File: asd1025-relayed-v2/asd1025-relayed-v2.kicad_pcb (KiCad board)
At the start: 2 copper layers, 61 x 40.6 mm, 20 parts, among them J1 DF3-12S-2DSA, J2 DF3-12S-2DSA, J3 DF3-12S-2DSA, J4 Conn_01x04_Male, J5 Conn_01x01_Female, J6 Conn_01x01_Female, K1 EC2-5NU, K2 EC2-5NU, K3 EC2-5NU, K4 EC2-5NU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

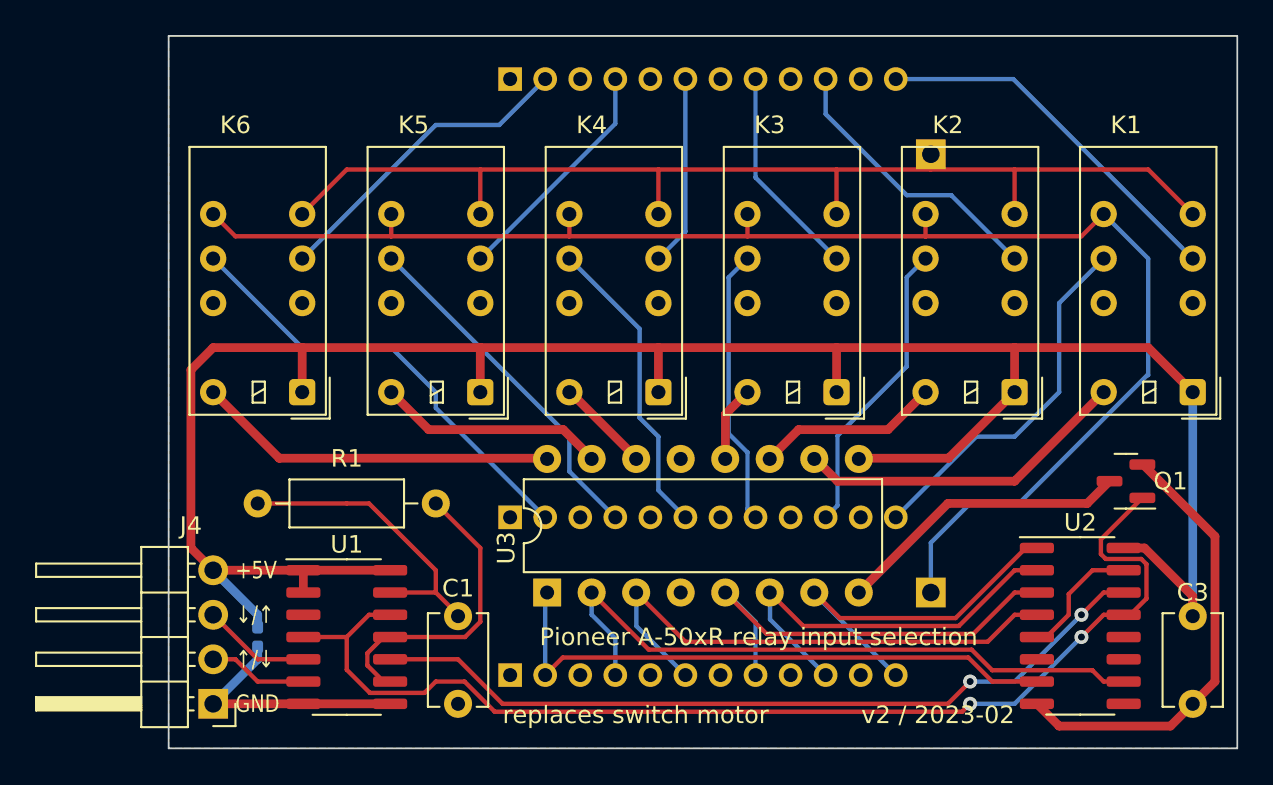
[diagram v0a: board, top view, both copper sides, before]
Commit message: fix mistake in v2 board about oscillator timing logic, nicer bottom silkscreen, no clock enabled signal needed anymore
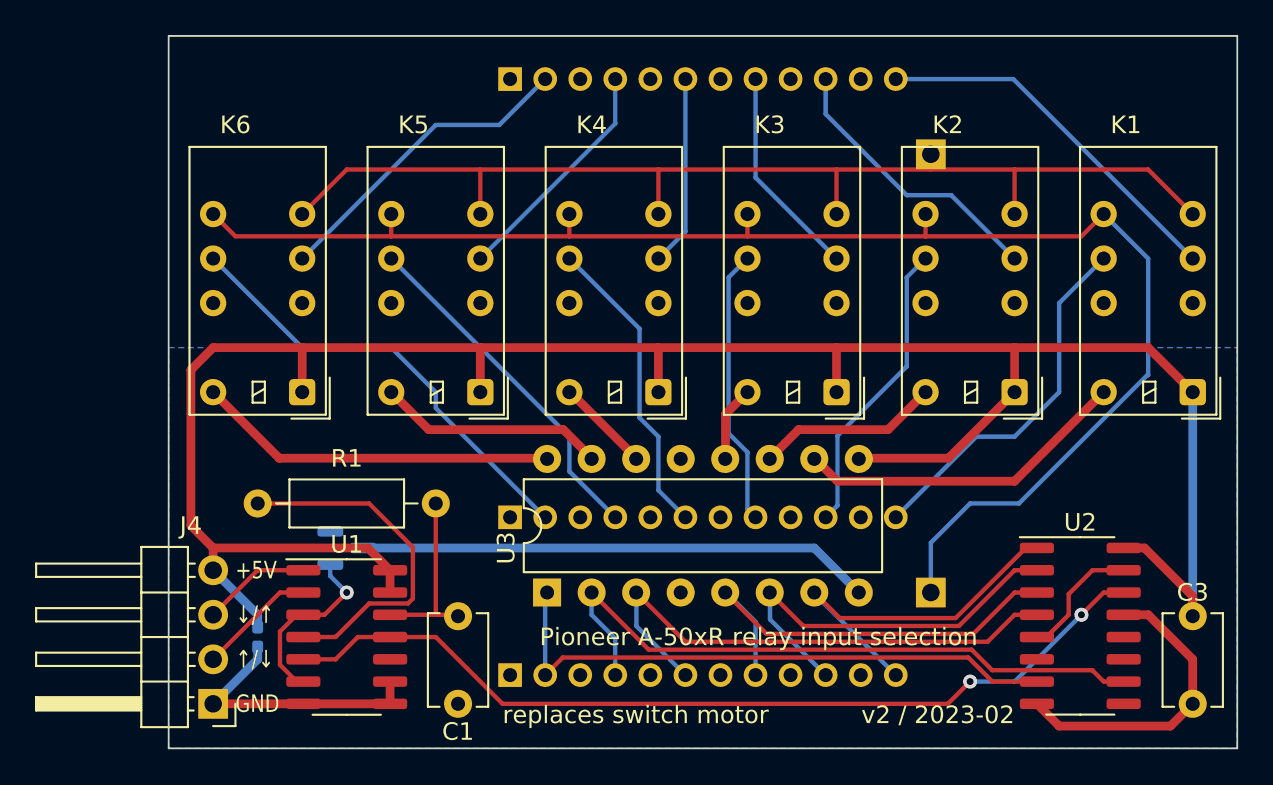
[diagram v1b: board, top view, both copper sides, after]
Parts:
- Q1: moved to B.Cu
- moved Q1 44.6 mm to (91.6, 145.4), turned to 0 degrees
- moved C1 5.00 mm to (97.9, 154.2), turned to 90 degrees
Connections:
- C1 pad 1: Net-(C1-Pad1) -> GNDREF
- C1 pad 2: GNDREF -> Net-(C1-Pad2)
- R1 pad 1: Net-(R1-Pad1) -> Net-(C1-Pad2)
- R1 pad 2: Net-(C1-Pad1) -> Net-(R1-Pad2)
- U1 pad 1: +5V -> Net-(J4-Pad3)
- U1 pad 10: Net-(U2-Pad14) -> unconnected-(U1-Pad10)
- U1 pad 11: Net-(R1-Pad1) -> Net-(U1-Pad11)
- U1 pad 12: Net-(Q1-Pad1) -> Net-(C1-Pad2)
- U1 pad 13: Net-(C1-Pad1) -> +5V
- U1 pad 2: +5V -> Net-(J4-Pad2)
- U1 pad 3: unconnected-(U1-Pad3) -> Net-(Q1-Pad1)
- U1 pad 4: Net-(Q1-Pad1) -> Net-(R1-Pad2)
- U1 pad 5: Net-(J4-Pad3) -> Net-(U1-Pad11)
- U1 pad 6: Net-(J4-Pad2) -> Net-(Q1-Pad1)
- U1 pad 9: Net-(R1-Pad1) -> GNDREF
- U2 pad 13: Net-(Q1-Pad1) -> GNDREF
- U2 pad 14: Net-(U2-Pad14) -> Net-(U1-Pad11)
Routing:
- net Net-(Q1-Pad1): track 66.2 -> 10.3 mm, vias 2 -> 1
- net Net-(U1-Pad11): track 0.00 -> 51.5 mm, vias 0 -> 2
- net Net-(U2-Pad14): track 45.5 -> 0.00 mm, vias 2 -> 0
- net Net-(R1-Pad2): track 0.00 -> 20.0 mm
- net Net-(C1-Pad1): track 17.5 -> 0.00 mm
- net Net-(R1-Pad1): track 17.4 -> 0.00 mm
- net Net-(Q1-Pad3): track 16.9 -> 29.3 mm
- net Net-(C1-Pad2): track 0.00 -> 10.3 mm
- net GNDREF: track 40.2 -> 33.5 mm
- net Net-(J4-Pad2): track 5.67 -> 6.72 mm
- net +5V: track 128.5 -> 129.0 mm

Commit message: change oscillator frequency to minimum to ensure 10ms between relai cut-off and on-switching
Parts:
- R1: value 150k -> 120k
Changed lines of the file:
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@@
       (effects (font (size 1 1) (thickness 0.15)))
     )
-    (fp_text value "150k" (at 5.08 2.37) (layer "F.Fab")
+    (fp_text value "120k" (at 5.08 2.37) (layer "F.Fab")
       (effects (font (size 1 1) (thickness 0.15)))
     )

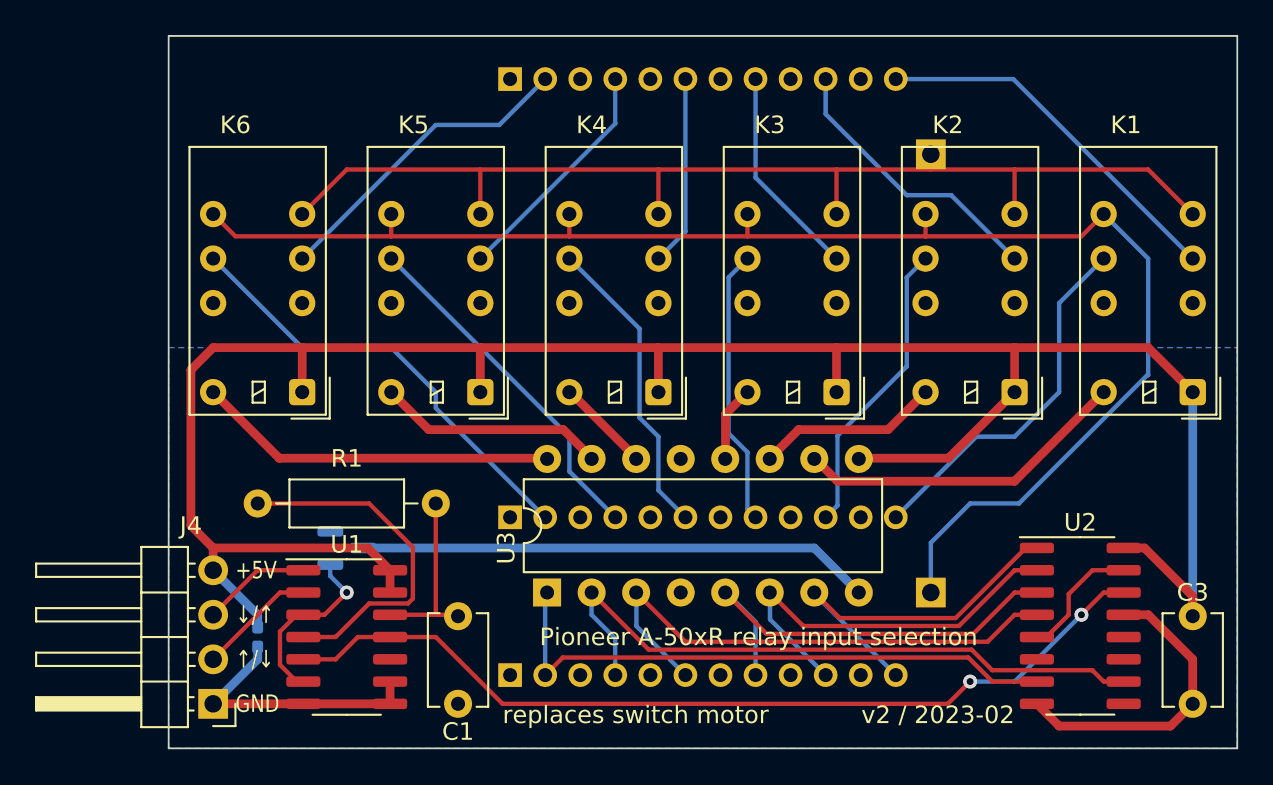
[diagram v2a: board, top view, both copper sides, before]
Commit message: fix v2: relays would switch by passing current through base-emittor-resistors in darlington array even if main transistor Q1 is off
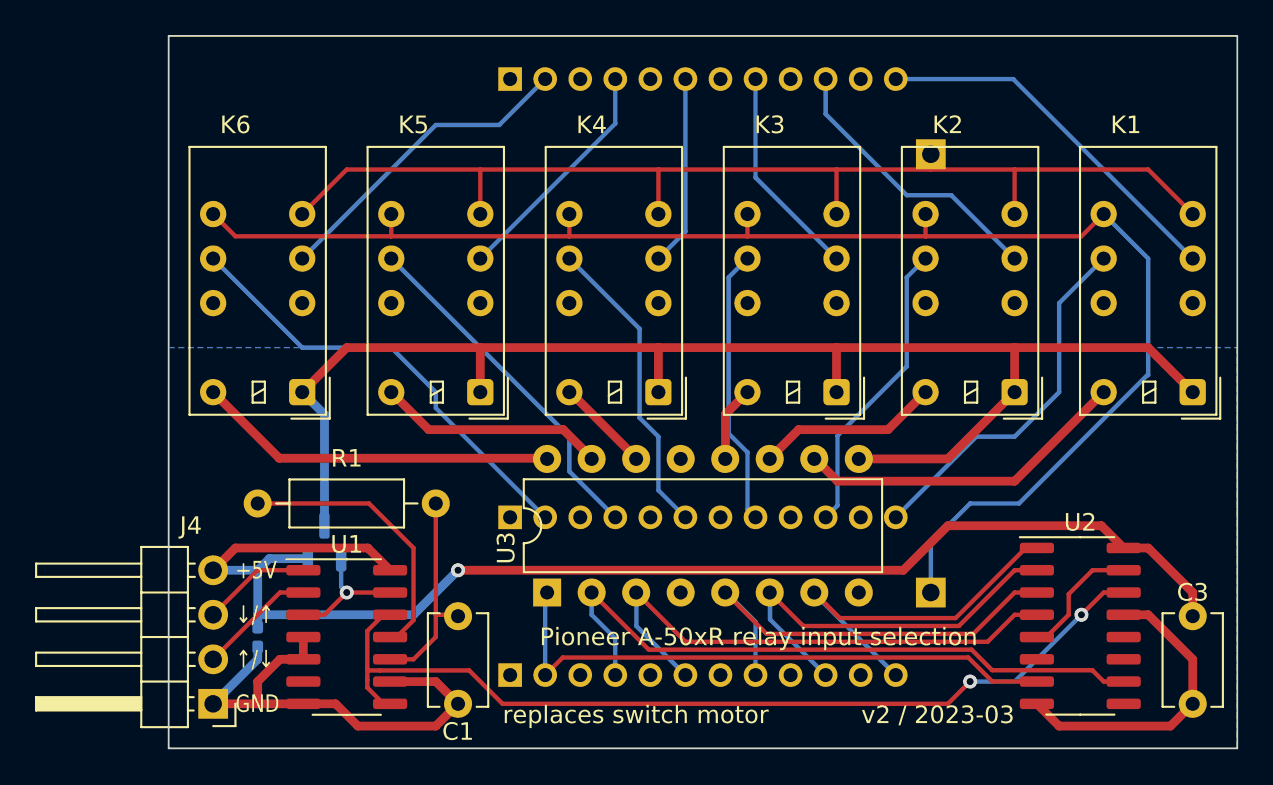
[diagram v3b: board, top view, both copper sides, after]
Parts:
- Q1: value DTC114E -> DTA123Y
- U1: value SN74HCS7266 -> SN74HCS86DR
- moved Q1 1.31 mm to (90.3, 145.0), turned to 90 degrees
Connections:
- K1 pad 1: +5V -> /R+
- K2 pad 1: +5V -> /R+
- K3 pad 1: +5V -> /R+
- K4 pad 1: +5V -> /R+
- K5 pad 1: +5V -> /R+
- K6 pad 1: +5V -> /R+
- Q1 pad 1: Net-(Q1-Pad1) -> Net-(U1-Pad3)
- Q1 pad 2: GNDREF -> +5V
- Q1 pad 3: Net-(Q1-Pad3) -> /R+
- U1 pad 10: unconnected-(U1-Pad10) -> Net-(C1-Pad2)
- U1 pad 11: Net-(U1-Pad11) -> Net-(R1-Pad2)
- U1 pad 12: Net-(C1-Pad2) -> Net-(U1-Pad12)
- U1 pad 13: +5V -> Net-(U1-Pad3)
- U1 pad 3: Net-(Q1-Pad1) -> Net-(U1-Pad3)
- U1 pad 4: Net-(R1-Pad2) -> GNDREF
- U1 pad 5: Net-(U1-Pad11) -> GNDREF
- U1 pad 6: Net-(Q1-Pad1) -> unconnected-(U1-Pad6)
- U1 pad 8: GNDREF -> Net-(U1-Pad12)
- U2 pad 14: Net-(U1-Pad11) -> Net-(U1-Pad12)
- U3 pad 8: Net-(Q1-Pad3) -> GNDREF
- U3 pad 9: +5V -> /R+
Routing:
- net /R+: track 0.00 -> 81.7 mm
- net Net-(U1-Pad12): track 0.00 -> 53.1 mm, vias 0 -> 2
- net Net-(U1-Pad11): track 51.5 -> 0.00 mm, vias 2 -> 0
- net +5V: track 129.0 -> 78.4 mm, vias 0 -> 1
- net Net-(Q1-Pad3): track 29.3 -> 0.00 mm
- net GNDREF: track 33.5 -> 46.9 mm
- net Net-(Q1-Pad1): track 10.3 -> 0.00 mm, vias 1 -> 0
- net Net-(U1-Pad3): track 0.00 -> 7.54 mm, vias 0 -> 1
- net Net-(R1-Pad2): track 20.0 -> 15.8 mm
- net Net-(C1-Pad2): track 10.3 -> 12.1 mm
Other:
- board text added: "v2 / 2023-03"
- board text removed: "v2 / 2023-02"
